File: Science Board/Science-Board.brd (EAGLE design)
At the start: 157.5 x 63.5 mm, 60 parts, among them J1 APPPP45_PCB_HORIZ_RIGHT_2HIGH, J2 APPPP45_PCB_HORIZ_RIGHT_2HIGH, J3 APPPP45_PCB_HORIZ_RIGHT_2HIGH, U3 SN74AHCT125

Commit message: Fixed messed up files
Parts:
- removed C6: 1uF, rcl:C0805
- removed H1, H2, H5: MOUNTING_HOLE#6, MRDT-Hardware:#6_SCREW
- removed LASER: SL02-HORIZ, MRDT-Connectors:MOLEX-70551-0001
- removed R12, R16, R18, R20: 10k, rcl:R0805
- removed R13, R17, R19, R21: 19.3k, rcl:R0805
- removed R2: 21.8k, rcl:M0805
- removed R3: 4.7k, rcl:M0805
- removed SOIL-SENSORS: SL04, MRDT-Connectors:MOLEX_SL_04_TH
- removed U$3: AP7365-WG-7DICT-ND, MRDT-ICs:SOT-25
- removed U$4: BSS136N, MRDT-Semiconductors:PG-SOT23-3
- removed WEATHER_SENSORS: SL08, MRDT-Connectors:MOLEX-70551-0007
- added C13: 4.7u, rcl:C0805
- added C14: 10u, rcl:C0805
- added J10: SL02, MRDT-Connectors:MOLEX-70543-0001
- added J11, J4, J5, J6, J9: SL03, MRDT-Connectors:MOLEX-70543-0002
- added J7, J8: SL04VERT, MRDT-Connectors:MOLEX-70543-0003
- added LED1: (no value), led:CHIP-LED0805
- added Q1: BSS123, transistor-small-signal:SOT23
- added R14: 1k, rcl:M0805
- added R15, R23, R25, R27: 10k, rcl:R0805
- added R22, R24, R26, R28: 19.3k, rcl:R0805
- added U$10: LB1930MC, Custom:SOIC10
- added U$11: NDS355AN, transistors:SOT-23
- U$2: value DRV8838DSGT -> LXDC2HN; device MRDT-ICs:8-WFDFN -> MRDT-ICs:4-SMD
- moved H3 105.4 mm to (110.5, 56.1)
- moved SPEC-MOTOR 93.6 mm to (144.2, 49.2), turned to 270 degrees
- moved C5 83.7 mm to (135.1, 52.8), turned to 0 degrees
- moved C3 67.1 mm to (96.5, 20.6), turned to 270 degrees
- moved OKI-5V-EXT 65.7 mm to (92.2, 19.1), turned to 0 degrees
- moved C4 63.5 mm to (95.1, 15.5)
- moved U$5 58.8 mm to (88.0, 50.6)
- moved U$9 57.4 mm to (181.0, 42.7)
- moved U$2 56.2 mm to (114.3, 28.4), turned to 0 degrees
- moved J1 52.9 mm to (42.4, 33.4)
- moved J2 52.9 mm to (42.4, 25.4)
- moved J3 52.9 mm to (42.4, 17.4)
- moved R1 44.8 mm to (81.3, 45.7), turned to 270 degrees
- moved DIODE1 37.5 mm to (99.6, 50.2), turned to 0 degrees
- moved DIODE2 37.0 mm to (118.7, 50.2), turned to 0 degrees
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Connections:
- removed net N$15: R20.2, WEATHER_SENSORS.P$4
- removed net N$16: R18.2, WEATHER_SENSORS.P$6
- removed net N$17: R16.2, WEATHER_SENSORS.P$5
- removed net N$18: R2.1, R3.2, U$3.P$4
- removed net N$5: C5.2, R2.2, U$2.P$1, U$3.P$5
- new net IN1: U$1.PM5, U$10.IN1
- new net IN2: U$1.PB3, U$10.IN2
- new net N$20: LED1.A, R14.1
- new net N$21: J4.3, R15.2
- new net N$22: J6.3, R27.2
- new net N$6: J8.2, R25.2
- new net UV-3.3: C14.1, J8.1, J8.4, U$2.P$3
- net 3V: now also J10.2; no longer LASER.P$2
- net 3V-ENABLE: no longer U$3.P$3
- net 5V-EXT: now also C5.1, J4.1, J5.1, J6.1, U$10.VCC; no longer C6.2, SOIL-SENSORS.1, U$3.P$1, U$8.8, WEATHER_SENSORS.P$1
- net 5V-INT: now also C13.1, J11.2, J7.4, J9.2, R14.2, U$2.P$1, U$2.P$2, U$8.8; no longer U$2.P$8
- net EN: no longer U$2.P$5
- net GAS-A: now also R15.1, R22.2, U$1.PL3; no longer R16.1, R17.2, U$1.PK1
- net GND: now also C13.2, C14.2, C5.2, DIODE1.1, DIODE2.1, J11.3, J4.2, J5.2, J6.2, J7.3, J8.3, J9.3, LED1.C, R22.1, R24.1, R26.1, R28.1, U$10.P-GND, U$10.S-GND, U$11.2; no longer C5.1, C6.1, DIODE1.P$1, DIODE2.P$1, R13.1, R17.1, R19.1, R21.1, R3.1, SOIL-SENSORS.2, U$3.P$2, U$4.P$2, WEATHER_SENSORS.P$8
- net HUMIDITY-A: now also R27.1, R28.2, U$1.PP2; no longer R12.1, R13.2, U$1.PK3
- net LASER-CTRL: now also U$1.PD4, U$11.1; no longer U$1.PQ3/PA2, U$4.P$3
- net LEVEL-EN: now also U$1.PM2; no longer U$1.PA5
- net LIGHT-A: now also R25.1, R26.2, U$1.PG1; no longer R20.1, R21.2, U$1.PK0
- net N$1: now also SPEC-MOTOR.2, U$10.OUT2; no longer SPEC-MOTOR.P$1, U$2.P$2
- net N$2: now also SPEC-MOTOR.1, U$10.OUT1; no longer SPEC-MOTOR.P$2, U$2.P$3
- net N$3: now also J10.1, U$11.3; no longer LASER.P$1, U$4.P$1
- net N$4: now also DIODE1.2; no longer DIODE1.P$2
- net N$7: now also J5.3, R23.2; no longer R12.2, WEATHER_SENSORS.P$7
- net N$9: now also DIODE2.2; no longer DIODE2.P$2
- net PHASE: no longer U$2.P$6
- net PHOTO-IN: now also U$1.PD2; no longer U$1.PD0
- net PHOTO-IN-2: now also U$1.PD3; no longer U$1.PD1
- net PRESSURE-SCL-3V3: now also U$1.PM0; no longer U$1.PN5
- net PRESSURE-SCL-5V: now also J7.1; no longer WEATHER_SENSORS.P$3
- net PRESSURE-SDA-3V3: now also U$1.PP5; no longer U$1.PN4
- net PRESSURE-SDA-5V: now also J7.2; no longer WEATHER_SENSORS.P$2
- net SERVO-CAROUSEL: now also U$1.PL2; no longer U$1.PM4
- net SERVO-FLAP: now also U$1.PL0; no longer U$1.PM5
- net SLEEP: no longer U$2.P$7
- net SOIL-MOISTURE: now also J9.1; no longer SOIL-SENSORS.4
- net SOIL-TEMP: now also J11.1, U$1.PK5; no longer SOIL-SENSORS.3, U$1.PB5
- net TEMP-A: now also R23.1, R24.2, U$1.PN3; no longer R18.1, R19.2, U$1.PK2
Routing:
- net 5V-EXT: track 243.1 -> 155.5 mm, vias 1 -> 4
- net GAS-A: track 45.8 -> 7.64 mm
- net LIGHT-A: track 52.5 -> 15.7 mm, vias 0 -> 1
- net 5V-INT: track 191.0 -> 162.5 mm, vias 4 -> 0
- net LASER-CTRL: track 41.7 -> 16.5 mm
- net PHOTO-IN: track 46.5 -> 21.5 mm, vias 2 -> 0
- net 3.3V: track 44.2 -> 21.7 mm, vias 2 -> 1
- net LEVEL-EN: track 9.87 -> 30.8 mm, vias 0 -> 1
- net SOIL-MOISTURE: track 23.7 -> 43.9 mm, vias 0 -> 1
- net UV-3.3: track 0.00 -> 17.6 mm
- net HUMIDITY-A: track 29.2 -> 11.7 mm
- net PRESSURE-SDA-3V3: track 14.3 -> 30.5 mm, vias 0 -> 1
- net IN2: track 0.00 -> 15.7 mm
- net EN: track 14.6 -> 0.00 mm
- net PRESSURE-SCL-3V3: track 15.5 -> 29.8 mm, vias 0 -> 1
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- removed copper zone on layer 1, net N$5
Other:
- board size 157.5 x 63.5 mm -> 104.1 x 55.9 mm

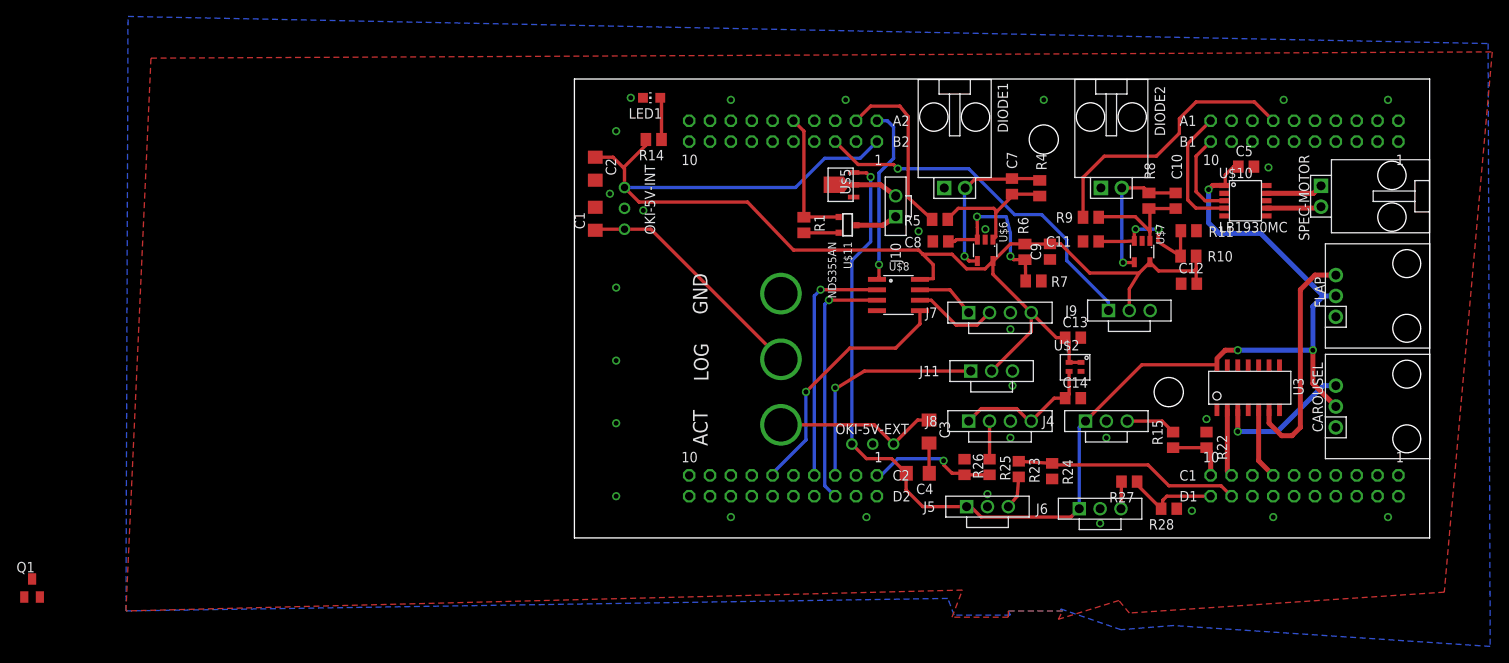
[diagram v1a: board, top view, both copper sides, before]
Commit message: Fixed traces
rearranged the sensor traces i did at 2 in the mornig to be less crap. also added katie's signiture, and fixed drc errors
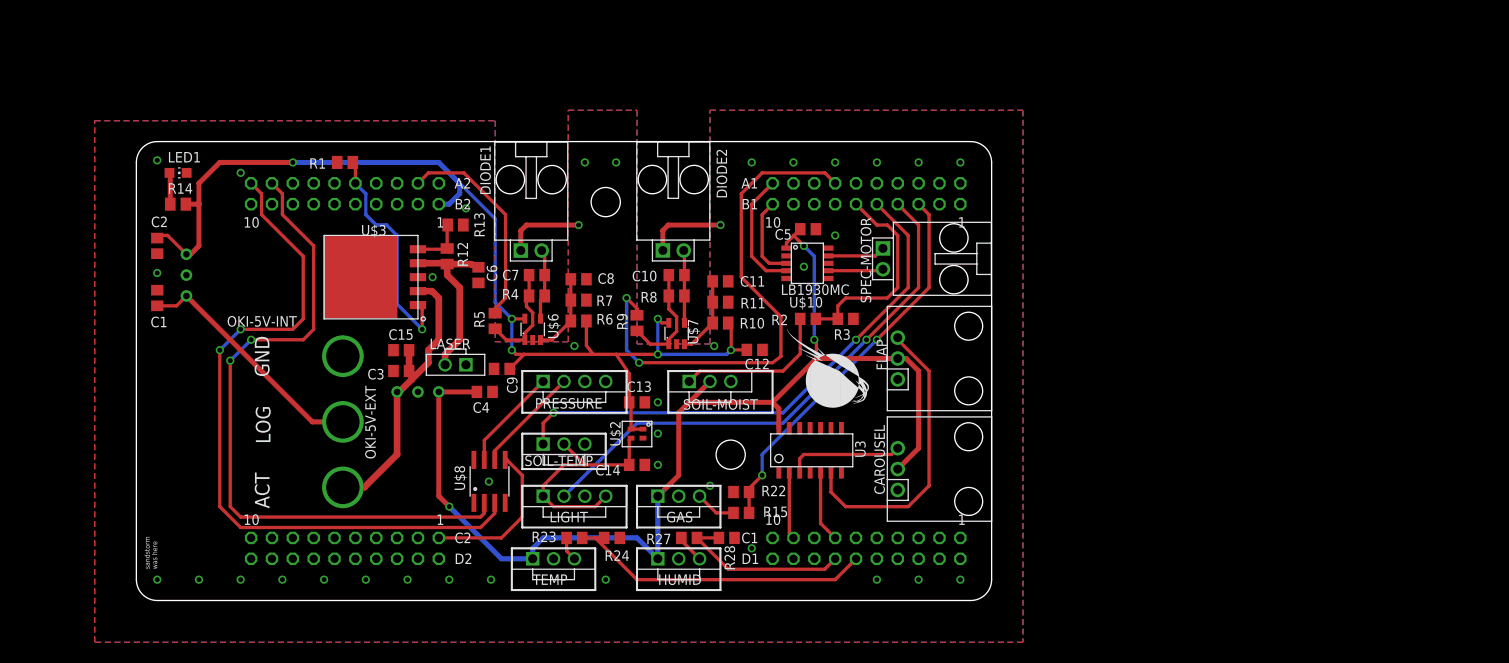
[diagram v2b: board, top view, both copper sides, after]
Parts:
- removed J1, J2, J3: APPPP45_PCB_HORIZ_RIGHT_2HIGH, MRDT-Connectors:APP45_PCB_HORIZ_RIGHT_2HIGH
- removed J10: SL02, MRDT-Connectors:MOLEX-70543-0001
- removed J11, J4, J5, J6, J9: SL03, MRDT-Connectors:MOLEX-70543-0002
- removed J7, J8: SL04VERT, MRDT-Connectors:MOLEX-70543-0003
- removed Q1: BSS123, transistor-small-signal:SOT23
- removed R25: 10k, rcl:R0805
- removed R26: 19.3k, rcl:R0805
- removed U$11: NDS355AN, transistors:SOT-23
- removed U$5: TLV1117LV30DCYR, MRDT-ICs:TO-243AA
- removed U$9: MADISON-CHILDRESS, sig:MADISON-CHLDRESS-SIG
- added ACT, GND, LOG: APPPP45_PCB_HORIZ_RIGHT_2HIGH, MRDT-Connectors:APP45_PCB_HORIZ_RIGHT_2HIGH
- added C15: 33uF, rcl:C0805
- added C6: 22uF, rcl:C0805
- added GAS, HUMID, SOIL-MOIST, SOIL-TEMP, TEMP: SL03, MRDT-Connectors:MOLEX-70543-0002
- added LASER: SL02, MRDT-Connectors:MOLEX-70543-0001
- added LIGHT, PRESSURE: SL04VERT, MRDT-Connectors:MOLEX-70543-0003
- added R12: 3.92k, rcl:M0805
- added R13: 5k, rcl:M0805
- added R2: 10k, rcl:R0805
- added R3: 19.3k, rcl:R0805
- added U$3: BA00DD0WHFP-TR, MRDT-ICs:TO-263-6
- added U$4: KATIE-BRINKER, sig:KATIE-BRINKER-SIG
- C1, C2, C3, C4: device rcl:C1206 -> rcl:C0805
- R1: value (none) -> 10k
- moved C9 68.2 mm to (44.5, 28.2), turned to 0 degrees
- moved C3 64.7 mm to (32.3, 27.9), turned to 180 degrees
- moved R4 62.6 mm to (48.8, 37.1), turned to 180 degrees
- moved C10 61.4 mm to (65.8, 39.6), turned to 0 degrees
- moved OKI-5V-EXT 60.8 mm to (31.8, 25.4), turned to 180 degrees
- moved C7 58.8 mm to (48.8, 39.6), turned to 0 degrees
- moved R8 58.7 mm to (65.8, 37.1), turned to 180 degrees
- moved R14 58.4 mm to (5.08, 48.3), turned to 0 degrees
- moved LED1 58.4 mm to (5.08, 52.1), turned to 270 degrees
- moved R11 57.7 mm to (71.1, 36.3)
- moved R10 57.6 mm to (71.1, 33.8)
- moved U$7 57.5 mm to (65.8, 32.5), turned to 0 degrees
- moved U$8 57.1 mm to (40.6, 12.7), turned to 0 degrees
- moved R22 57.0 mm to (73.7, 13.2), turned to 0 degrees
- moved R9 56.7 mm to (61.0, 33.8), turned to 90 degrees
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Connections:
- removed net 3V: J10.2, U$5.2
- new net N$25: R12.1, R13.2, U$3.P$5
- net 3.3V: no longer U$1.+3V3_1, U$1.+3V3_2
- net 5V-EXT: now also GAS.1, HUMID.1, SOIL-MOIST.2, TEMP.1; no longer J4.1, J5.1, J6.1, U$5.3
- net 5V-INT: no longer J11.2, J7.4, J9.2, U$8.8
- net ACT-12V: now also ACT.P$2, C15.1, U$3.P$2; no longer J3.P$2
- net GAS-A: now also U$1.PE0; no longer U$1.PL3
- net GND: now also C15.2, C6.2, GAS.2, GND.P$2, HUMID.2, LASER.1, LIGHT.3, PRESSURE.3, R13.1, R3.1, SOIL-MOIST.3, SOIL-TEMP.3, TEMP.2, U$3.P$3, U$3.P$6; no longer J1.P$2, J11.3, J4.2, J5.2, J6.2, J7.3, J8.3, J9.3, R26.1, U$11.2, U$5.1
- net HUMIDITY-A: now also U$1.PD0; no longer U$1.PP2
- net LASER-CTRL: now also U$3.P$1; no longer U$11.1
- net LEVEL-EN: now also U$1.PG1; no longer U$1.PM2
- net LIGHT-A: now also LIGHT.2, U$1.PE1; no longer R25.1, R26.2, U$1.PG1
- net LOGIC-12V: now also LOG.P$2; no longer J2.P$2
- net N$21: now also GAS.3; no longer J4.3
- net N$22: now also HUMID.3; no longer J6.3
- net N$3: now also C6.1, LASER.2, R12.2, U$3.P$4; no longer J10.1, U$11.3
- net N$6: now also R2.2, SOIL-MOIST.1; no longer J8.2, R25.2
- net N$7: now also TEMP.3; no longer J5.3
- net PRESSURE-SCL-3V3: now also U$1.PN5; no longer U$1.PM0
- net PRESSURE-SCL-5V: now also PRESSURE.1; no longer J7.1
- net PRESSURE-SDA-3V3: now also U$1.PN4; no longer U$1.PP5
- net PRESSURE-SDA-5V: now also PRESSURE.2; no longer J7.2
- net SOIL-MOISTURE: now also R2.1, R3.2, U$1.PE3; no longer J9.1, U$1.PB4
- net SOIL-TEMP: now also SOIL-TEMP.1, U$1.PE2; no longer J11.1, U$1.PK5
- net TEMP-A: now also U$1.PD1; no longer U$1.PN3
- net UV-3.3: now also LIGHT.1, LIGHT.4, SOIL-TEMP.2; no longer J8.1, J8.4
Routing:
- net PRESSURE-SDA-3V3: track 30.5 -> 86.4 mm, vias 1 -> 2
- net PRESSURE-SCL-3V3: track 29.8 -> 82.3 mm, vias 1 -> 2
- net LIGHT-A: track 15.7 -> 64.9 mm
- net GAS-A: track 7.64 -> 47.2 mm, vias 0 -> 2
- net SOIL-TEMP: track 27.8 -> 65.6 mm, vias 1 -> 2
- net PHOTO-IN-2: track 33.8 -> 63.5 mm, vias 0 -> 2
- net 5V-INT: track 162.5 -> 135.4 mm, vias 0 -> 6
- net 3.3V: track 21.7 -> 0.00 mm, vias 1 -> 0
- net SOIL-MOISTURE: track 43.9 -> 25.5 mm, vias 1 -> 0
- net N$3: track 5.09 -> 21.1 mm
- net ACT-12V: track 20.2 -> 36.1 mm
- net 5V-EXT: track 155.5 -> 140.6 mm, vias 4 -> 3
- net N$6: track 4.64 -> 19.2 mm
- net LEVEL-EN: track 30.8 -> 19.2 mm, vias 1 -> 0
- net GND: track 7.93 -> 19.5 mm, vias 27 -> 38
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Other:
- outline, holes or cut-outs redrawn
- board text added: "Missouri S&T Mars Rover Design Team Science Board 2017 | Gryphon | Rev 2 Katie Brinker"
- board text added: "sandstorm was here"
- board text removed: "Missouri S&T Mars Rover Design Team Science Board 2017 | Rev 1 Madison Childress"
